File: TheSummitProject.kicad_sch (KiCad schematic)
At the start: 18 parts, among them IC1 STM32U5F7VJT6, J1 Cortex SWD, SW1 SW_SPDT

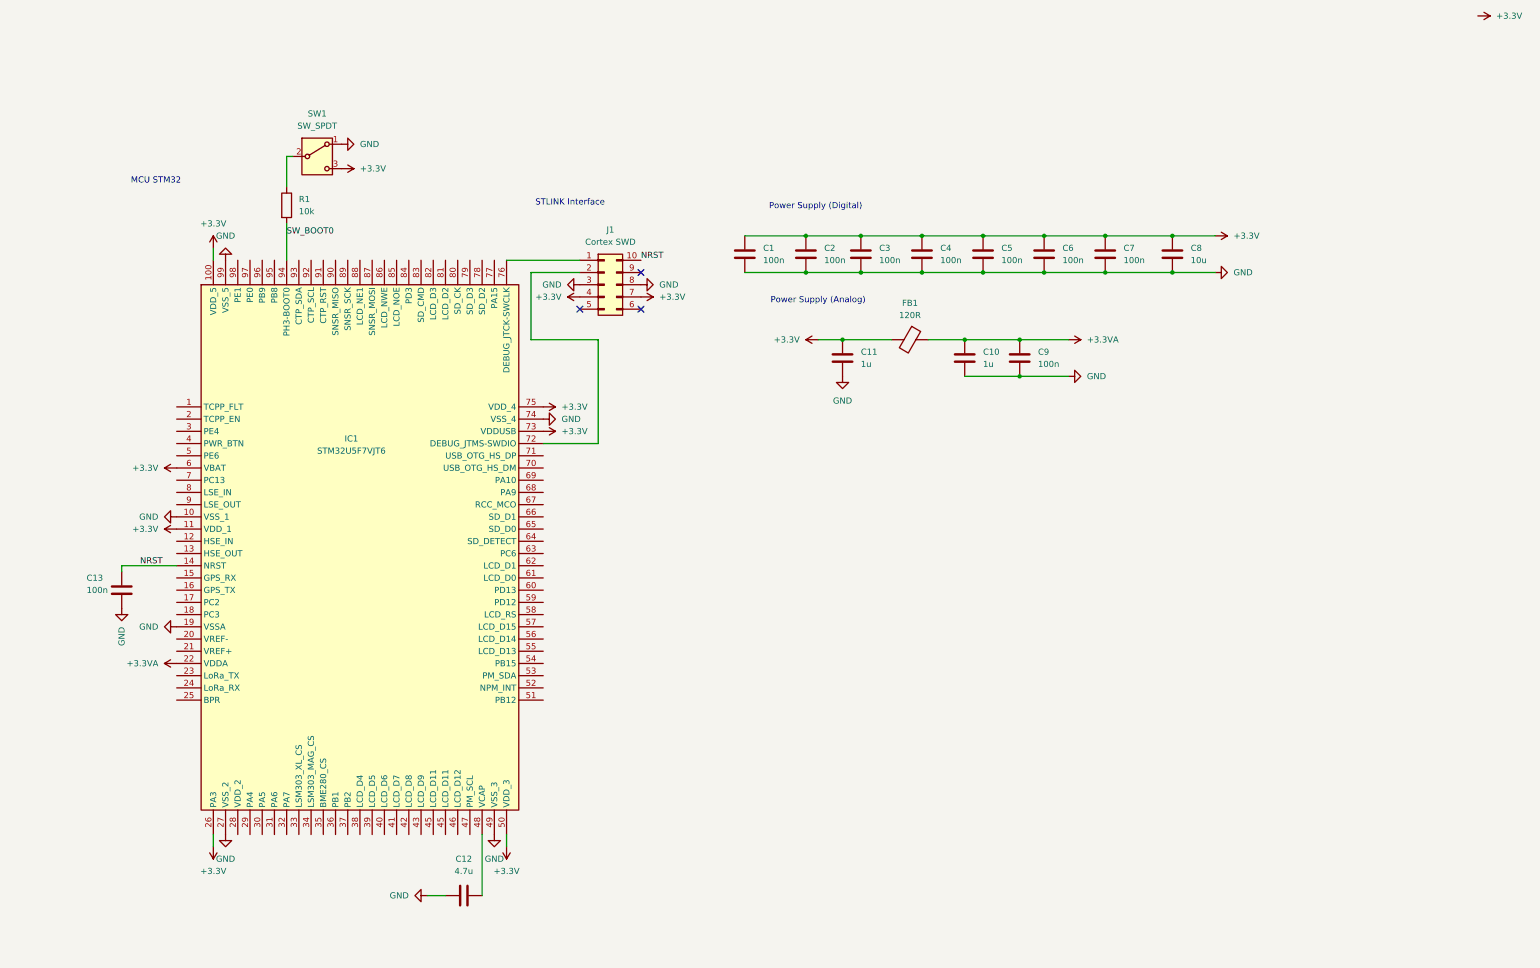
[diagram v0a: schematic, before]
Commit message: Added clocks
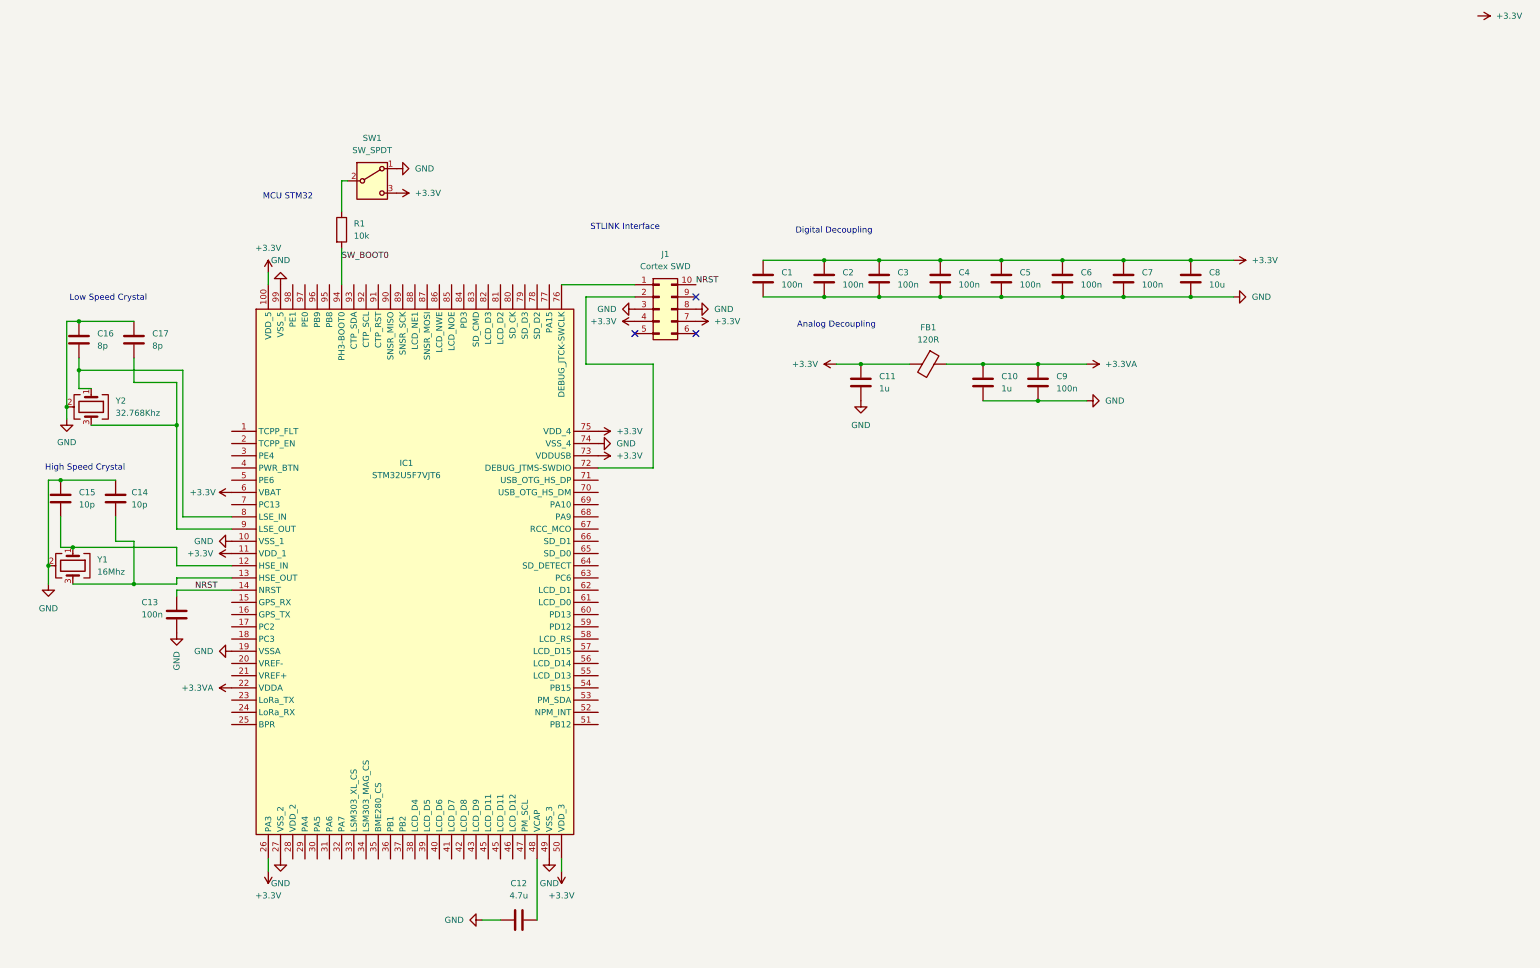
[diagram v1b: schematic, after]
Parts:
- added C14, C15: 10p, symbol Device:C
- added C16, C17: 8p, symbol Device:C
- added Y1: 16Mhz, symbol Device:Crystal_GND24
- added Y2: 32.768Khz, symbol Device:Crystal_GND24
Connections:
- net GND: now also C14.1, C15.1, C16.1, C17.1, Y1.2 (G), Y1.4 (G), Y2.2 (G), Y2.4 (G)
- net at IC1.12 (HSE_IN): now also C15.2, Y1.1
- net at IC1.13 (HSE_OUT): now also C14.2, Y1.3
- net at IC1.8 (LSE_IN): now also C16.2, Y2.1
- net at IC1.9 (LSE_OUT): now also C17.2, Y2.3
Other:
- note added: "Analog Decoupling"
- note added: "Digital Decoupling"
- note added: "High Speed Crystal"
- note added: "Low Speed Crystal"
- note removed: "Power Supply (Analog)"
- note removed: "Power Supply (Digital)"
- moved on the sheet: C1, C10, C11, C12, C13, C2, C3, C4, C5, C6, C7, C8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

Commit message: Added extra decouplings for analog, connected VREF
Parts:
- added C18: 1u, symbol Device:C
- added C19: 100n, symbol Device:C
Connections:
- net +3.3VA: now also IC1.21 (VREF+), C18.1, C19.1
- net GND: now also IC1.20 (VREF-), C18.2, C19.2
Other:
- moved on the sheet: C10, C11, C9, FB1

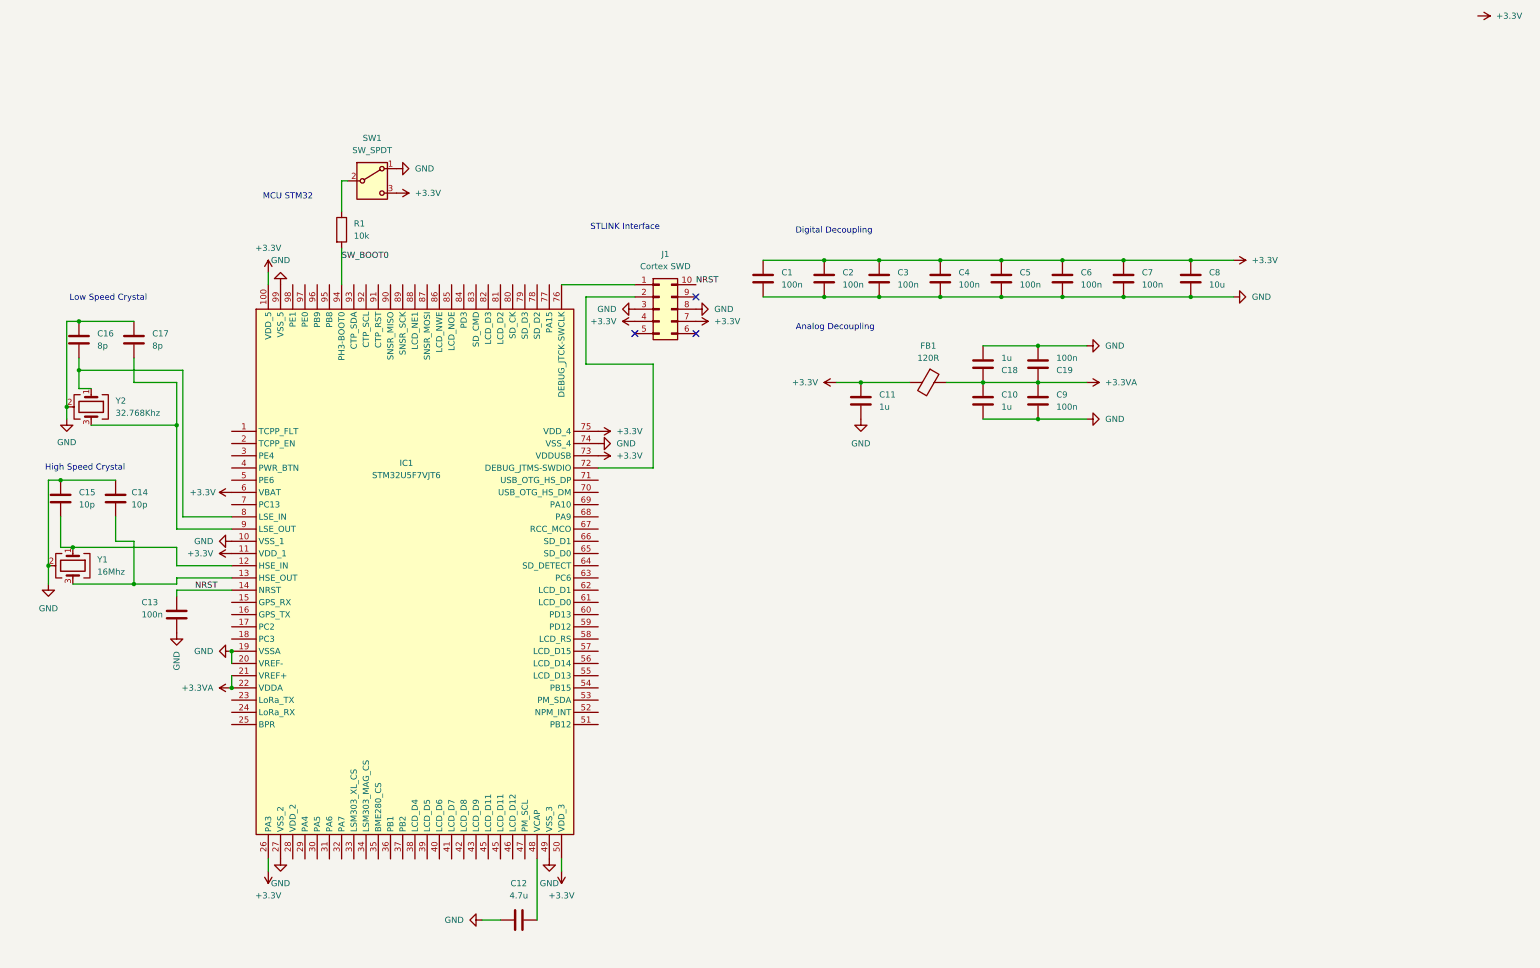
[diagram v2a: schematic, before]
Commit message: added markings labels
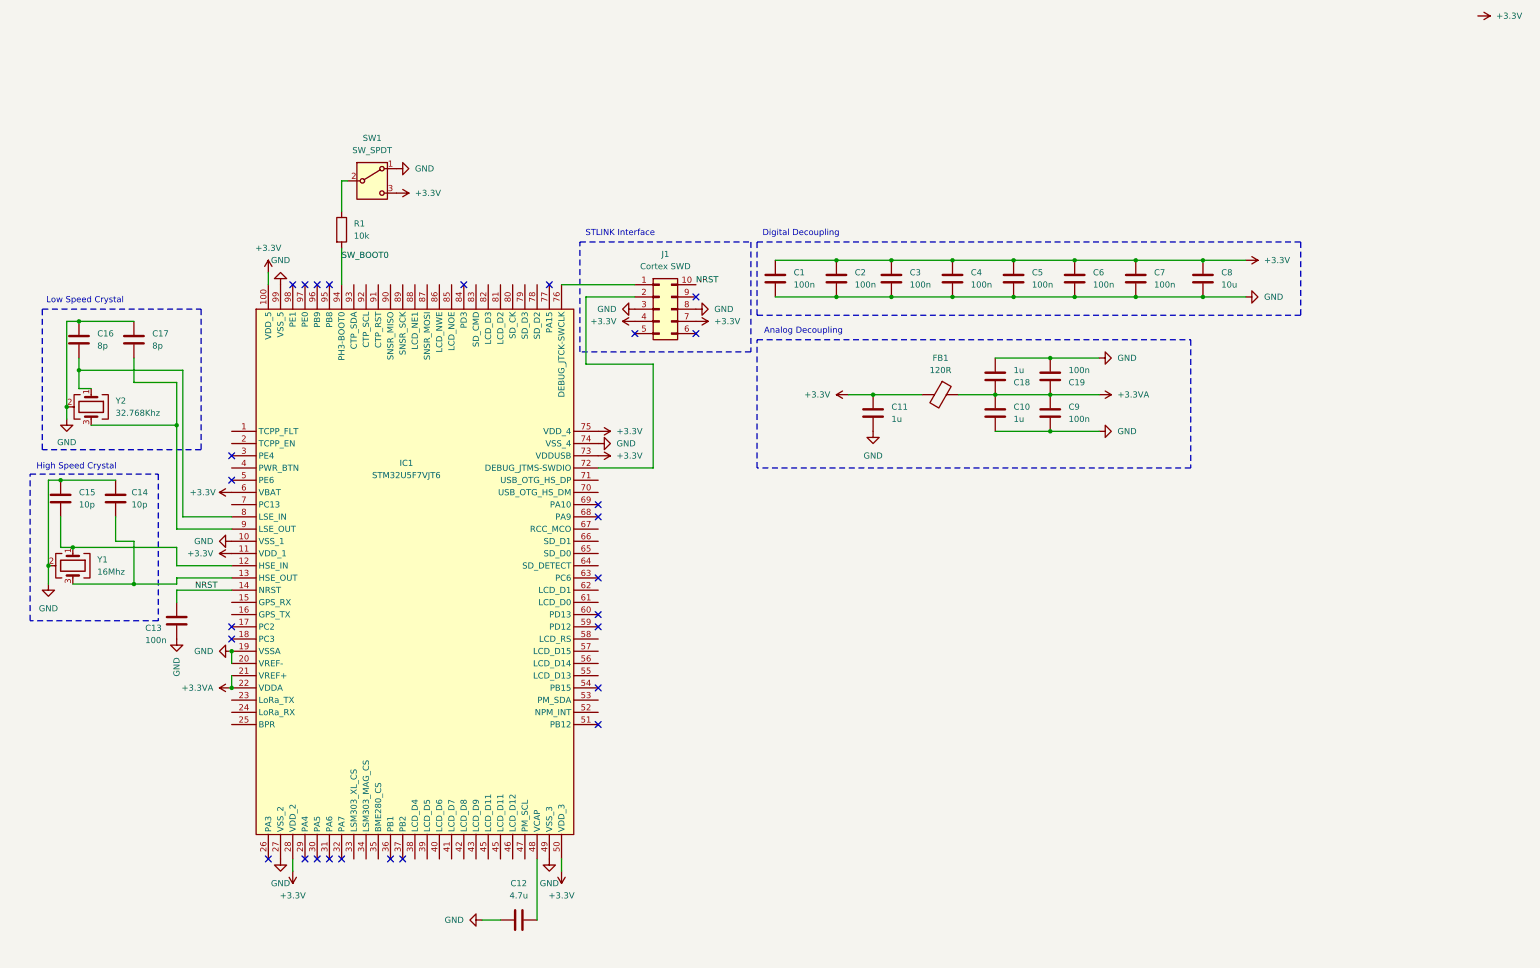
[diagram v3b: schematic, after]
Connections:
- net +3.3V: now also IC1.28 (VDD_2); no longer IC1.26 (PA3)
- no-connect marks 3 -> 27
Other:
- note removed: "MCU STM32"
- title: (none) -> MCU
- moved on the sheet: C1, C10, C11, C13, C18, C19, C2, C3, C4, C5, C6, C7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

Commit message: added PMIC schematic
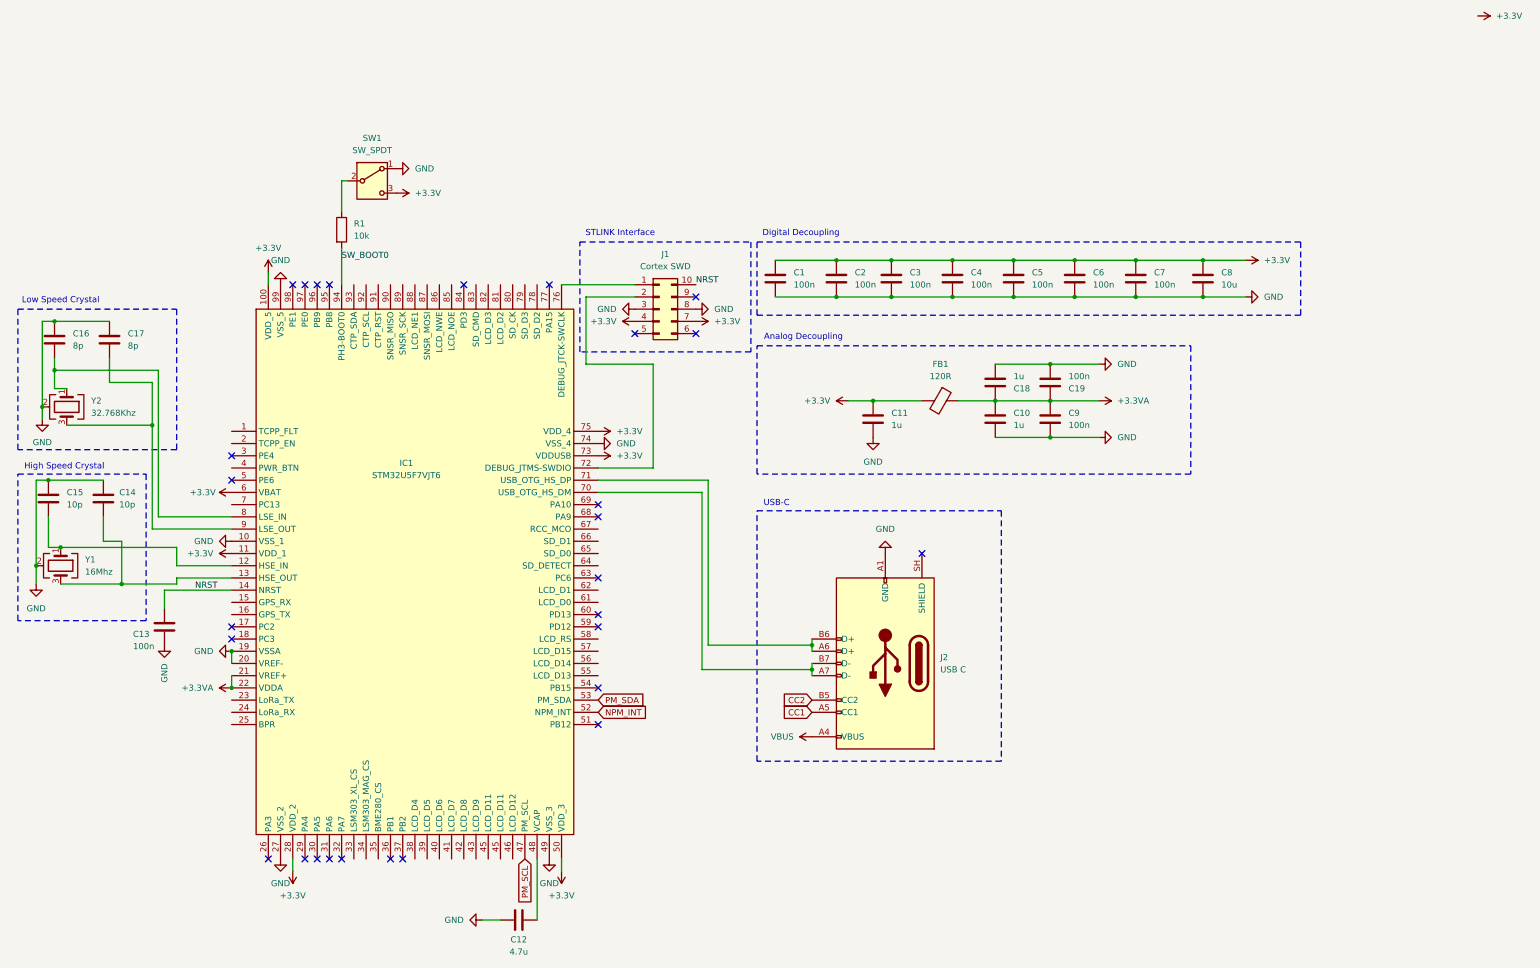
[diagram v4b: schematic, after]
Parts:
- added J2: USB C, symbol Connector:USB_C_Receptacle_USB2.0_14P
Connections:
- net GND: now also J2.A1 (GND), J2.A12 (GND), J2.B1 (GND), J2.B12 (GND)
- net PM_SCL: now reaches IC1.47 (PM_SCL)
- net NPM_INT: now reaches IC1.52 (NPM_INT)
- net PM_SDA: now reaches IC1.53 (PM_SDA)
- net at IC1.70 (USB_OTG_HS_DM): now also J2.A7 (D-), J2.B7 (D-)
- net at IC1.71 (USB_OTG_HS_DP): now also J2.A6 (D+), J2.B6 (D+)
- new net CC1: J2.A5 (CC1)
- new net CC2: J2.B5 (CC2)
- new net VBUS: J2.A4 (VBUS), J2.A9 (VBUS), J2.B4 (VBUS), J2.B9 (VBUS)
- no-connect marks 27 -> 28
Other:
- note added: "USB-C"
- title: MCU -> STM32U5F7
- moved on the sheet: C10, C11, C13, C14, C15, C16, C17, C18, C19, C9, FB1, Y1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

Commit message: fixed ERC warnings, finalized PMIC
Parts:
- IC1: footprint QFP50P1600X1600X160-100N -> TheSummitProject:QFP50P1600X1600X160-100N
